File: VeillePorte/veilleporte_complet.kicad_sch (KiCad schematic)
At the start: 47 parts, among them J10 P-MFC, J19 Conn_01x02_Socket, J21 UART2 / RUI3, J22 SWD, J23 CABLE MODULE VL53L4CD, J3 Conn_01x02_Pin, J4 Conn_01x02_Pin, SW1 RESET, U1 RAK3172(H) / EU868, U2 BQ25570

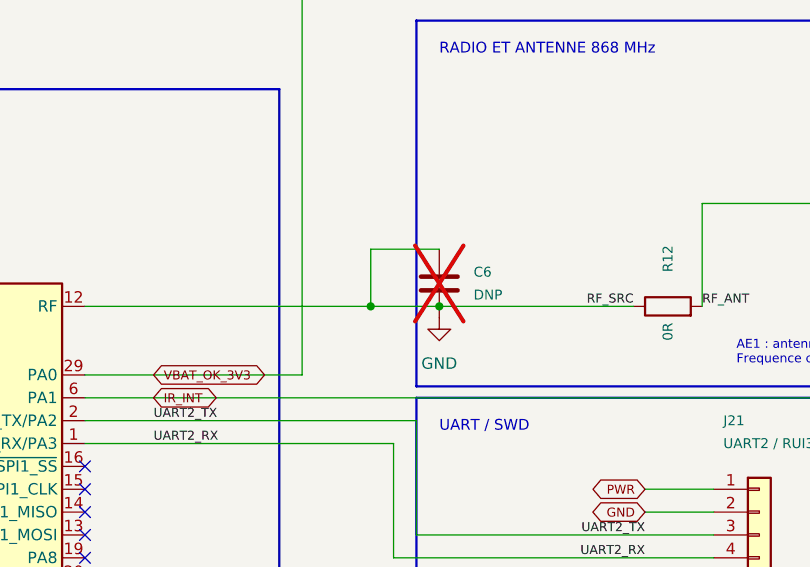
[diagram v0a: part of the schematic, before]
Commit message: Raccorde C6 en shunt sur RF
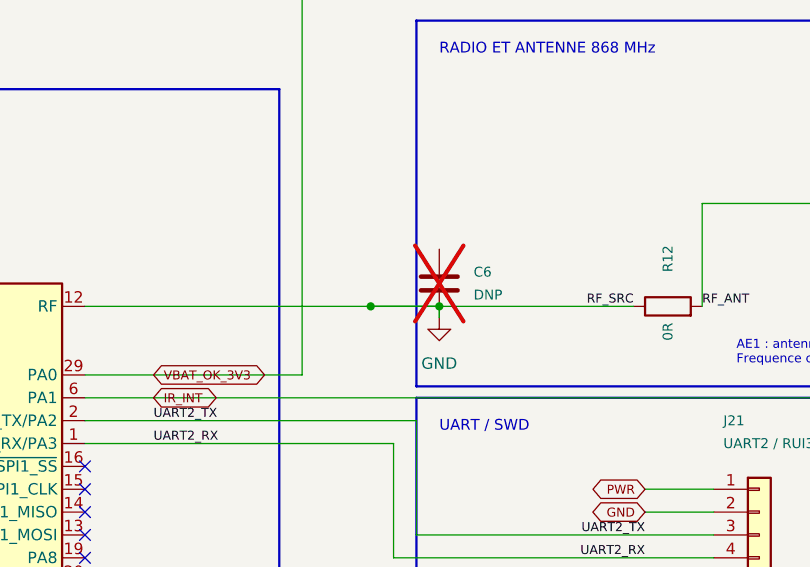
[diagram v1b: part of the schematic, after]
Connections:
- net GND: now also R12.1, U1.12 (RF)
- removed net RF_SRC: C6.1, R12.1, U1.12 (RF)
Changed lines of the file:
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@@
 	)
 	(wire
-		(pts (xy 438.15 52.07) (xy 438.15 45.72))
+		(pts (xy 438.15 52.07) (xy 445.77 52.07))
 		(stroke (width 0) (type default))
 	)
 	(wire
-		(pts (xy 438.15 45.72) (xy 445.77 45.72))
+		(pts (xy 445.77 52.07) (xy 445.77 53.34))
 		(stroke (width 0) (type default))
 	)

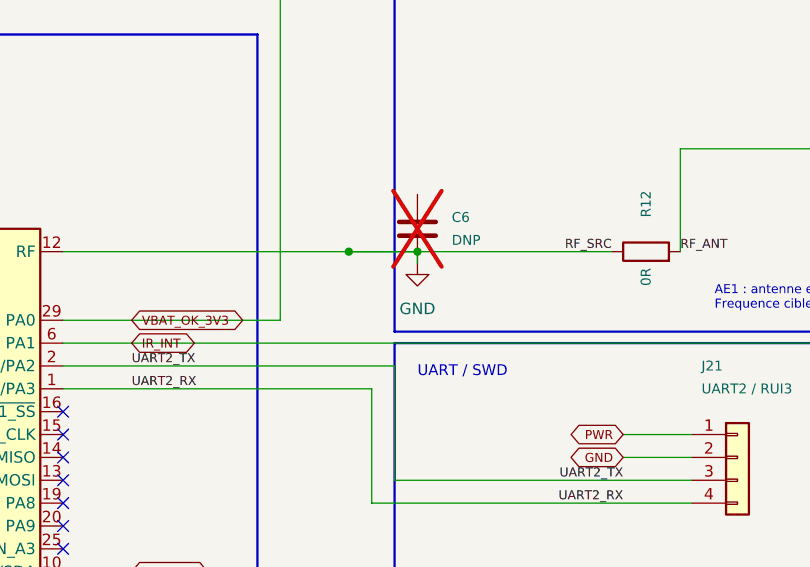
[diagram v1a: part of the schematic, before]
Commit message: Nettoie et unifie le projet KiCad VeillePorte
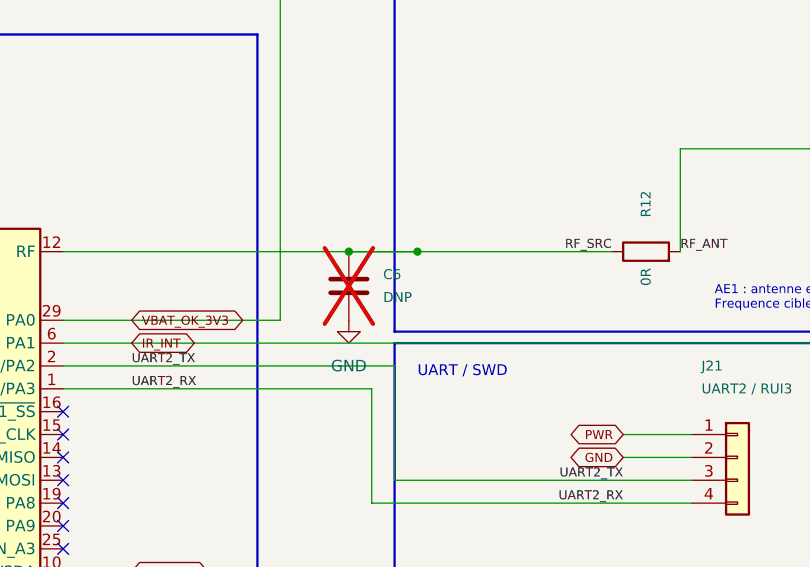
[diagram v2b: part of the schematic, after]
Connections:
- net GND: no longer R12.1, U1.12 (RF)
- net RF_SRC: now reaches C6.1
- net RF_SRC: now also R12.1, U1.12 (RF)
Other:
- moved on the sheet: C6
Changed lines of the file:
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@@
 	(symbol
 		(lib_id "power:GND")
-		(at 445.77 53.34 0)
+		(at 438.15 59.69 0)
 		(unit 1)
 		(body_style 1)
@@
 		(fields_autoplaced yes)
 		(property "Reference" "#PWR063"
-			(at 445.77 59.69 0)
+			(at 438.15 66.04 0)
 			(hide yes)
 			(show_name no)
@@
 		)
 		(property "Value" "GND"
-			(at 445.77 58.42 0)
+			(at 438.15 64.77 0)
 			(show_name no)
 			(do_not_autoplace no)
@@
 		)
 		(property "Footprint" ""
-			(at 445.77 53.34 0)
-			(hide yes)
-			(show_name no)
-			(do_not_autoplace no)
-			(effects
-				(font
-					(size 1.27 1.27)
-				)
-			)
-		)
-		(property "Datasheet" ""
-			(at 445.77 53.34 0)
+			(at 438.15 59.69 0)
+			(hide yes)
+			(show_name no)
+			(do_not_autoplace no)
+			(effects
+				(font
+					(size 1.27 1.27)
+				)
+			)
+		)
+		(property "Datasheet" ""
+			(at 438.15 59.69 0)
 			(hide yes)
 			(show_name no)
@@
 		)
 		(property "Description" "Power symbol creates a global label with name \"GND\" , ground"
-			(at 445.77 53.34 0)
+			(at 438.15 59.69 0)
 			(hide yes)
 			(show_name no)
@@
 	(symbol
 		(lib_id "Device:C")
-		(at 445.77 49.53 0)
+		(at 438.15 55.88 0)
 		(unit 1)
 		(body_style 1)
@@
 		(dnp yes)
 		(property "Reference" "C6"
-			(at 449.58 48.26 0)
+			(at 441.96 54.61 0)
 			(show_name no)
 			(do_not_autoplace no)
@@
 		)
 		(property "Value" "DNP"
-			(at 449.58 50.8 0)
+			(at 441.96 57.15 0)
 			(show_name no)
 			(do_not_autoplace no)
@@
 		)
 		(property "Footprint" "Capacitor_SMD:C_0603_1608Metric"
-			(at 440.69 49.53 0)
+			(at 433.07 55.88 0)
 			(hide yes)
 			(show_name no)
@@
 		)
 		(property "Datasheet" "https://www.pololu.com/product/3692"
-			(at 440.69 49.53 0)
+			(at 433.07 55.88 0)
 			(hide yes)
 			(show_name no)
@@
 		)
 		(property "Description" ""
-			(at 445.77 49.53 0)
+			(at 438.15 55.88 0)
 			(show_name no)
 			(do_not_autoplace no)
@@
 		(stroke (width 0) (type default))
 	)
-	(wire
-		(pts (xy 445.77 52.07) (xy 445.77 53.34))
-		(stroke (width 0) (type default))
-	)

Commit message: Router VeillePorte en quatre couches avec GND In2 et exports 3D
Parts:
- J10: value P-MFC -> PANNEAU SOLAIRE; footprint TerminalBlock_Phoenix:TerminalBlock_Phoenix_MKDS-3-2-5.08_1x02_P5.08mm_Horizontal -> VeillePorte_Connecteurs:Solar_Wires_2x_D1.0_P5.08
- J22: footprint Connector_PinHeader_2.54mm:PinHeader_1x05_P2.54mm_Vertical -> VeillePorte_Connecteurs:SWD_1x05_P2.54_VeillePorte
- U1: footprint RF_Module:RAK3172 -> VeillePorte_Modules:RAK3172_VeillePorte
- U2: footprint Package_DFN_QFN:QFN-20-1EP_3.5x3.5mm_P0.5mm_EP2x2mm -> VeillePorte_Modules:BQ25570_VeillePorte
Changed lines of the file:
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@@
 		(rev "0.6")
 		(company "Amira")
-		(comment 1 "Module Pololu 3692 externe ; supercapacite 4 V ; PCB a realiser")
+		(comment 1 "Module Pololu 3692 externe ; supercapacite 4 V ; PCB 4 couches route - RF a revalider")
 	)
 	(polyline
@@
 	(wire
 		(pts
-			(xy 351.79 125.73) (xy 474.98 125.73)
+			(xy 351.79 125.73) (xy 411.48 125.73)
 		)
 		(stroke
@@
 	(wire
 		(pts
-			(xy 474.98 125.73) (xy 474.98 115.57)
-		)
-		(stroke
-			(width 0)
-			(type default)
-		)
-	)
-	(wire
-		(pts
 			(xy 440.69 113.03) (xy 476.25 113.03)
 		)
@@
 			)
 		)
-		(property "Footprint" "RF_Module:RAK3172"
+		(property "Footprint" "VeillePorte_Modules:RAK3172_VeillePorte"
 			(at 386.08 74.93 0)
 			(hide yes)
@@
 			)
 		)
-		(property "Footprint" "Connector_PinHeader_2.54mm:PinHeader_1x05_P2.54mm_Vertical"
+		(property "Footprint" "VeillePorte_Connecteurs:SWD_1x05_P2.54_VeillePorte"
 			(at 481.33 110.49 0)
 			(hide yes)
@@
 			)
 		)
-		(property "Footprint" "Package_DFN_QFN:QFN-20-1EP_3.5x3.5mm_P0.5mm_EP2x2mm"
+		(property "Footprint" "VeillePorte_Modules:BQ25570_VeillePorte"
 			(at 160.02 91.44 0)
 			(hide yes)
@@
 			)
 		)
-		(property "Value" "P-MFC"
+		(property "Value" "PANNEAU SOLAIRE"
 			(at 29.21 80.01 0)
 			(show_name no)
@@
 			)
 		)
-		(property "Footprint" "TerminalBlock_Phoenix:TerminalBlock_Phoenix_MKDS-3-2-5.08_1x02_P5.08mm_Horizontal"
+		(property "Footprint" "VeillePorte_Connecteurs:Solar_Wires_2x_D1.0_P5.08"
 			(at 29.21 76.2 0)
 			(hide yes)
